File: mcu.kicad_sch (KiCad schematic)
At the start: 31 parts, among them J8 Conn_ARM_SWD_TagConnect_TC203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, J9 Conn_01x05_Pin, SW2 Reset, U1 ${ALTIUM_VALUE}, X1 ${ALTIUM_VALUE}, X2 ${ALTIUM_VALUE}

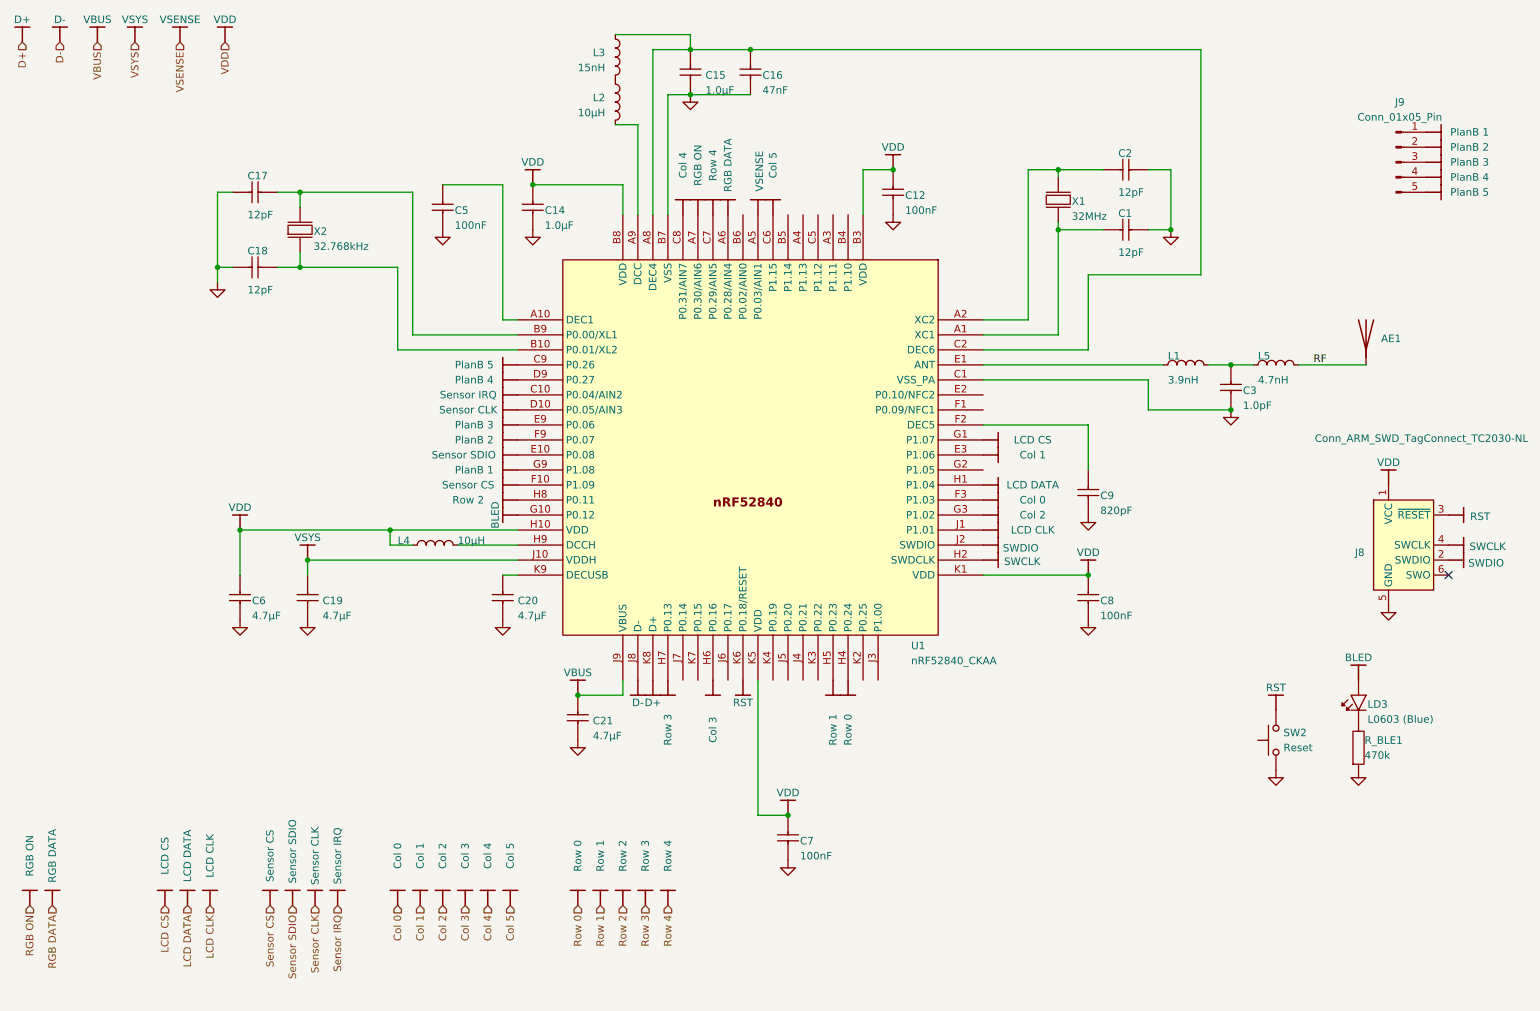
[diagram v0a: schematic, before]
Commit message: Reworking the MCU schematics sheet into QIAA package
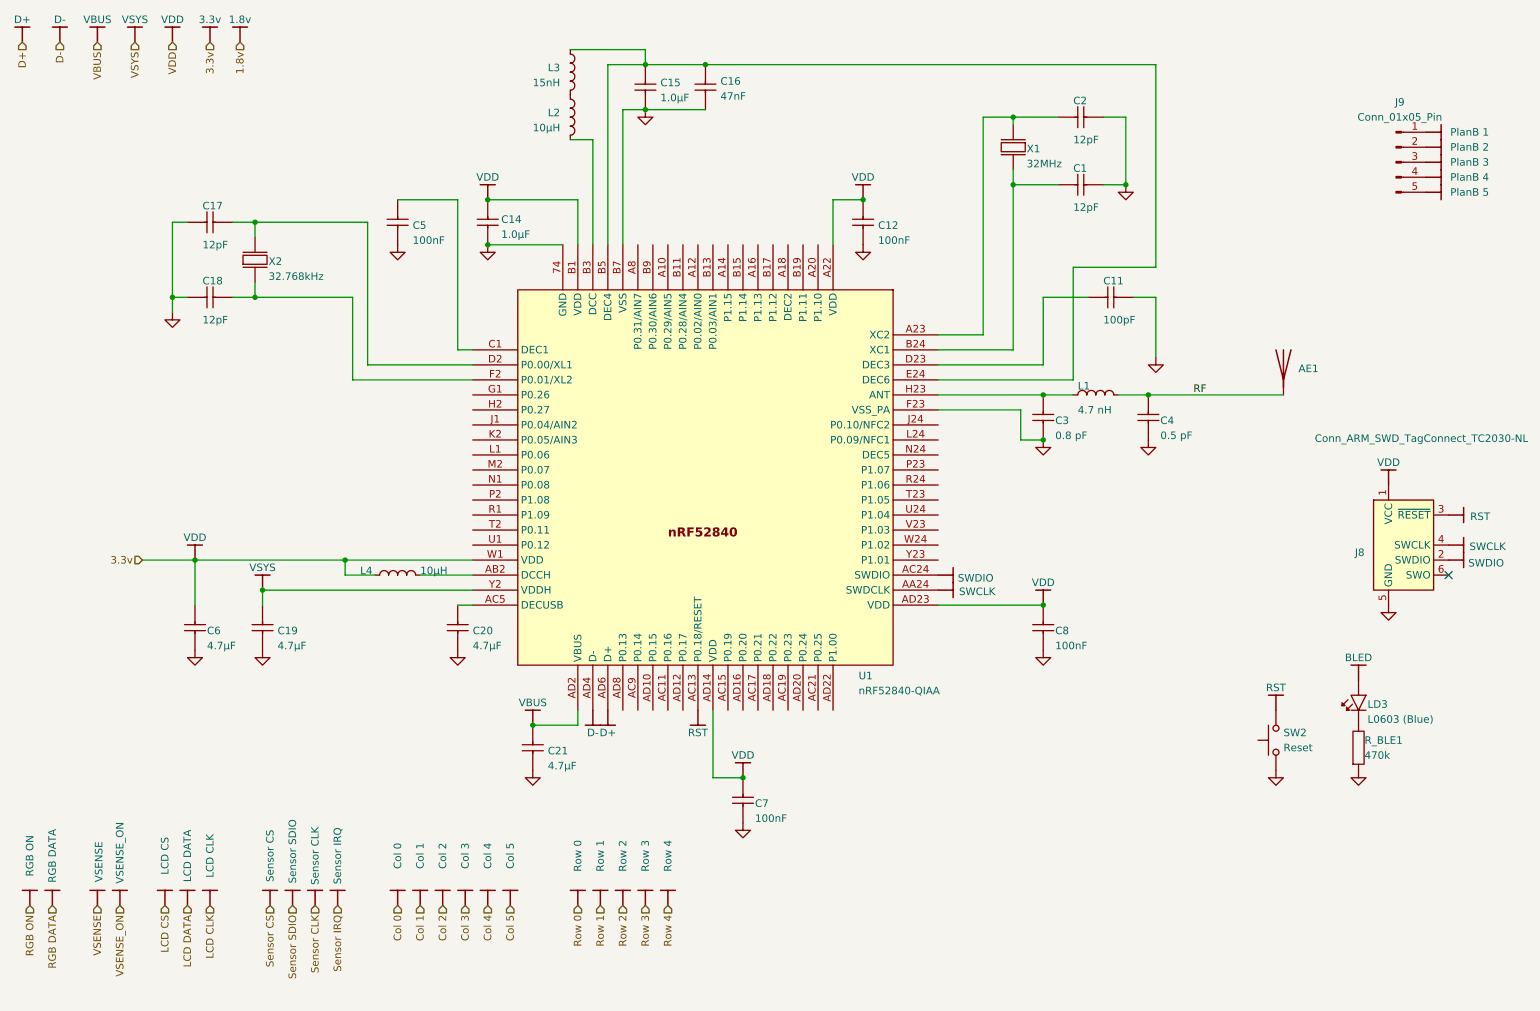
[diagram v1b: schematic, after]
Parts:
- removed C1, C2: ${ALTIUM_VALUE}, Capacitor_SMD:C_0201_0603Metric, symbol Nordic Passive DB:root_0_CAP_Nordic Passive DB.DbLib
- removed C12, C16: ${ALTIUM_VALUE}, Passive:CAPC0603X03L_C, symbol Nordic Passive DB:root_3_CAP_Nordic Passive DB.DbLib
- removed C14, C19, C20, C21, C6: ${ALTIUM_VALUE}, Passive:CAPC1608X06L, symbol Nordic Passive DB:root_3_CAP_Nordic Passive DB.DbLib
- removed C15: ${ALTIUM_VALUE}, Passive:CAPC1608X06L, symbol Nordic Passive DB:root_1_CAP_Nordic Passive DB.DbLib
- removed C17, C18: ${ALTIUM_VALUE}, Capacitor_SMD:C_0201_0603Metric, symbol Nordic Passive DB:root_2_CAP_Nordic Passive DB.DbLib
- removed C3: ${ALTIUM_VALUE}, Capacitor_SMD:C_0201_0603Metric, symbol Nordic Passive DB:root_1_CAP_Nordic Passive DB.DbLib
- removed C5, C7, C8, C9: ${ALTIUM_VALUE}, Capacitor_SMD:C_0201_0603Metric, symbol Nordic Passive DB:root_3_CAP_Nordic Passive DB.DbLib
- removed L1: ${ALTIUM_VALUE}, Inductors$:INDC0603X03L_C, symbol Nordic Passive DB:root_0_IND_Nordic Passive DB.DbLib
- removed L2: ${ALTIUM_VALUE}, 0603:INDC1608X06L, symbol Nordic Passive DB:root_3_IND_Nordic Passive DB.DbLib
- removed L3: ${ALTIUM_VALUE}, 0402:INDC1005X04L, symbol Nordic Passive DB:root_3_IND_Nordic Passive DB.DbLib
- removed L4: ${ALTIUM_VALUE}, Passive:INDC1608X06L, symbol Nordic Passive DB:root_0_IND_Nordic Passive DB.DbLib
- removed L5: ${ALTIUM_VALUE}, Passive:INDC0603X03L_C, symbol Nordic Passive DB:root_0_IND_Nordic Passive DB.DbLib
- removed U1: ${ALTIUM_VALUE}, nRF Devices$:BGA94C35P10X10_352X356X50, symbol Nordic Active DB:root_0_nRF52840_CKAA_Nordic Active DB.DbLib
- removed X1: ${ALTIUM_VALUE}, Crystal:Crystal_SMD_1210-4Pin_1.2x1.0mm, symbol Nordic Discrete DB:root_1_XTAL_4-pin_grounded_Nordic Discrete DB.DbLib
- removed X2: ${ALTIUM_VALUE}, EXC-1210:XTAL_ECS32761210TR, symbol Nordic Discrete DB:root_3_XTAL_2-pin_Nordic Discrete DB.DbLib
- added C1, C11, C2: ${ALTIUM_VALUE}, CAPC1005X04L, symbol AltiumLib:root_0_CAP_AltiumLib.DbLib
- added C12, C16, C5, C7, C8: ${ALTIUM_VALUE}, CAPC1005X04L, symbol AltiumLib:root_3_CAP_AltiumLib.DbLib
- added C14, C19, C20, C21, C6: ${ALTIUM_VALUE}, CAPC1608X06L, symbol AltiumLib:root_3_CAP_AltiumLib.DbLib
- added C15: ${ALTIUM_VALUE}, CAPC1608X06L, symbol AltiumLib:root_1_CAP_AltiumLib.DbLib
- added C17, C18: ${ALTIUM_VALUE}, CAPC1005X04L, symbol AltiumLib:root_2_CAP_AltiumLib.DbLib
- added C3: 0.8 pF, CAPC1005X04L, symbol AltiumLib:root_1_CAP_AltiumLib.DbLib
- added C4: 0.5 pF, CAPC1005X04L, symbol AltiumLib:root_1_CAP_AltiumLib.DbLib
- added L1: 4.7 nH, INDC1005X04L, symbol AltiumLib:root_0_IND_AltiumLib.DbLib
- added L2: ${ALTIUM_VALUE}, INDC1608X06L, symbol AltiumLib:root_3_IND_AltiumLib.DbLib
- added L3: ${ALTIUM_VALUE}, INDC1005X04L, symbol AltiumLib:root_3_IND_AltiumLib.DbLib
- added L4: ${ALTIUM_VALUE}, INDC1608X06L, symbol AltiumLib:root_0_IND_AltiumLib.DbLib
- added U1: ${ALTIUM_VALUE}, AQFN50P700X700X85_HS-74N, symbol AltiumLib:root_0_nRF52840_QIAA_AltiumLib.DbLib
- added X1: ${ALTIUM_VALUE}, BT-XTAL_2016, symbol AltiumLib:root_1_XTAL_4-pin_grounded_AltiumLib.DbLib
- added X2: ${ALTIUM_VALUE}, XTAL_3215, symbol AltiumLib:root_3_XTAL_2-pin_AltiumLib.DbLib
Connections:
- net D+: now also U1.AD6 (D+)
- net D-: now also U1.AD4 (D-)
- net GND: now also C1.2, C11.2, C12.2, C14.2, C15.1, C16.2, C17.2, C18.2, C19.2, C2.2, C20.2, C21.2, C3.1, C4.1, C5.2, C6.2, C7.2, C8.2, U1.74 (GND), U1.B7 (VSS), U1.F23 (VSS_PA)
- net RF: now also C4.2, L1.2
- net RST: now also U1.AC13 (P0.18/RESET)
- net SWCLK: now also U1.AA24 (SWDCLK)
- net SWDIO: now also U1.AC24 (SWDIO)
- net VBUS: now also C21.1, U1.AD2 (VBUS)
- net VSYS: now also C19.1, U1.Y2 (VDDH)
- net VDD renamed 3.3v
- net 3.3v: now also C12.1, C14.1, C6.1, C7.1, C8.1, L4.1, U1.A22 (VDD), U1.AD14 (VDD), U1.AD23 (VDD), U1.B1 (VDD), U1.W1 (VDD)
- new net: L2.1, L3.2
- new net: L2.2, U1.B3 (DCC)
- new net: C17.1, U1.D2 (P0.00/XL1), X2.1 (inp)
- new net: C18.1, U1.F2 (P0.01/XL2), X2.2 (out)
- new net: C11.1, U1.D23 (DEC3)
- new net: C15.2, C16.1, L3.1, U1.B5 (DEC4), U1.E24 (DEC6)
- new net: C1.1, U1.B24 (XC1), X1.1 (inp)
- new net: C2.1, U1.A23 (XC2), X1.3 (out)
- new net: C5.1, U1.C1 (DEC1)
- new net: L4.2, U1.AB2 (DCCH)
- new net: C20.1, U1.AC5 (DECUSB)
- new net: C3.2, L1.1, U1.H23 (ANT)
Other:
- moved on the sheet: AE1

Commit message: Dumping the reference layouts into the PCB
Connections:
- net 3.3v renamed VDD
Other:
- note added: "bypass"
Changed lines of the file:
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@@
 	(generator_version "9.0")
 	(paper "A4")
+	(text "bypass"
+		(exclude_from_sim no)
+		(at 68.326 25.908 0)
+		(effects
+			(font
+				(size 1.27 1.27)
+			)
+		)
+	)
 	(junction
 		(at 109.22 142.24)
@@
 	(wire
 		(pts
+			(xy 68.58 29.21) (xy 69.85 29.21)
+		)
+		(stroke
+			(width 0)
+			(type default)
+		)
+	)
+	(wire
+		(pts
 			(xy 58.42 69.85) (xy 62.23 69.85)
 		)
@@
 	(wire
 		(pts
-			(xy 52.07 114.3) (xy 43.18 114.3)
+			(xy 43.18 114.3) (xy 52.07 114.3)
 		)
 		(stroke
@@
 	(hierarchical_label "1.8v"
 		(shape input)
-		(at 59.69 26.67 270)
+		(at 69.85 29.21 0)
 		(effects
 			(font
 				(size 1.27 1.27)
 			)
-			(justify right)
+			(justify left)
 		)
 	)
@@
 	(hierarchical_label "3.3v"
 		(shape input)
-		(at 54.61 26.67 270)
+		(at 43.18 114.3 180)
 		(effects
 			(font
@@
 		)
 	)
-	(hierarchical_label "3.3v"
+	(hierarchical_label "1.8v "
 		(shape input)
-		(at 43.18 114.3 180)
+		(at 68.58 29.21 180)
 		(effects
 			(font
@@
 	(symbol
 		(lib_id "npm1100_caax_config1-altium-import:VBUS_BAR")
-		(at 59.69 26.67 180)
-		(unit 1)
-		(exclude_from_sim no)
-		(in_bom yes)
-		(on_board yes)
-		(dnp no)
-		(property "Reference" "#PWR048"
-			(at 59.69 26.67 0)
-			(effects
-				(font
-					(size 1.27 1.27)
-				)
-				(hide yes)
-			)
-		)
-		(property "Value" "1.8v"
-			(at 59.69 22.86 0)
-			(effects
-				(font
-					(size 1.27 1.27)
-				)
-			)
-		)
-		(property "Footprint" ""
-			(at 59.69 26.67 0)
-			(effects
-				(font
-					(size 1.27 1.27)
-				)
-			)
-		)
-		(property "Datasheet" ""
-			(at 59.69 26.67 0)
-			(effects
-				(font
-					(size 1.27 1.27)
-				)
-			)
-		)
-		(property "Description" ""
-			(at 59.69 26.67 0)
-			(effects
-				(font
-					(size 1.27 1.27)
-				)
-			)
-		)
-		(pin ""
-		)
-		(instances
-			(project "plan-b"
-				(path "/3a835e6f-a660-4b38-a102-87841cdd95ed/5bb1d2f7-c8fd-447b-99e1-d61ef924696c"
-					(reference "#PWR048")
-					(unit 1)
-				)
-			)
-		)
-	)
-	(symbol
-		(lib_id "npm1100_caax_config1-altium-import:VBUS_BAR")
 		(at 68.58 172.72 180)
 		(unit 1)
@@
 					(unit 1)
 				)
-			)
-		)
-	)
-	(symbol
-		(lib_id "npm1100_caax_config1-altium-import:VBUS_BAR")
-		(at 54.61 26.67 180)
-		(unit 1)
-		(exclude_from_sim no)
-		(in_bom yes)
-		(on_board yes)
-		(dnp no)
-		(property "Reference" "#PWR0179"
-			(at 54.61 26.67 0)
-			(effects
-				(font
-					(size 1.27 1.27)
-				)
-				(hide yes)
-			)
-		)
-		(property "Value" "3.3v"
-			(at 54.61 22.86 0)
-			(effects
-				(font
-					(size 1.27 1.27)
-				)
-			)
-		)
-		(property "Footprint" ""
-			(at 54.61 26.67 0)
-			(effects
-				(font
-					(size 1.27 1.27)
-				)
-			)
-		)
-		(property "Datasheet" ""
-			(at 54.61 26.67 0)
-			(effects
-				(font
-					(size 1.27 1.27)
-				)
-			)
-		)
-		(property "Description" ""
-			(at 54.61 26.67 0)
-			(effects
-				(font
-					(size 1.27 1.27)
-				)
-			)
-		)
-		(pin ""
-		)
-		(instances
-			(project "plan-b"
-				(path "/3a835e6f-a660-4b38-a102-87841cdd95ed/5bb1d2f7-c8fd-447b-99e1-d61ef924696c"
-					(reference "#PWR0179")
-					(unit 1)
-				)

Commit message: Cleaning up more components
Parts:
- added C9: 820pF, CAPC1005X04L, symbol AltiumLib:root_3_CAP_AltiumLib.DbLib
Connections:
- net GND: now also C9.2
- net at U1.N24 (DEC5): now also C9.1
